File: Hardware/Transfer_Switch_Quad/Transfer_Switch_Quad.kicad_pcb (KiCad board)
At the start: 2 copper layers, 100 x 100 mm, 30 parts, among them J1 Relays, J10 RF1, J6 RF2, J7 RF3, J8 AMP, J9 RF4, K10 G2RL-1-E, K11 G2RL-1-E, K12 G2RL-1-E, K13 G2RL-1-E, K14 G2RL-1-E, K15 G2RL-1-E, K16 G2RL-1-E, K9 G2RL-1-E

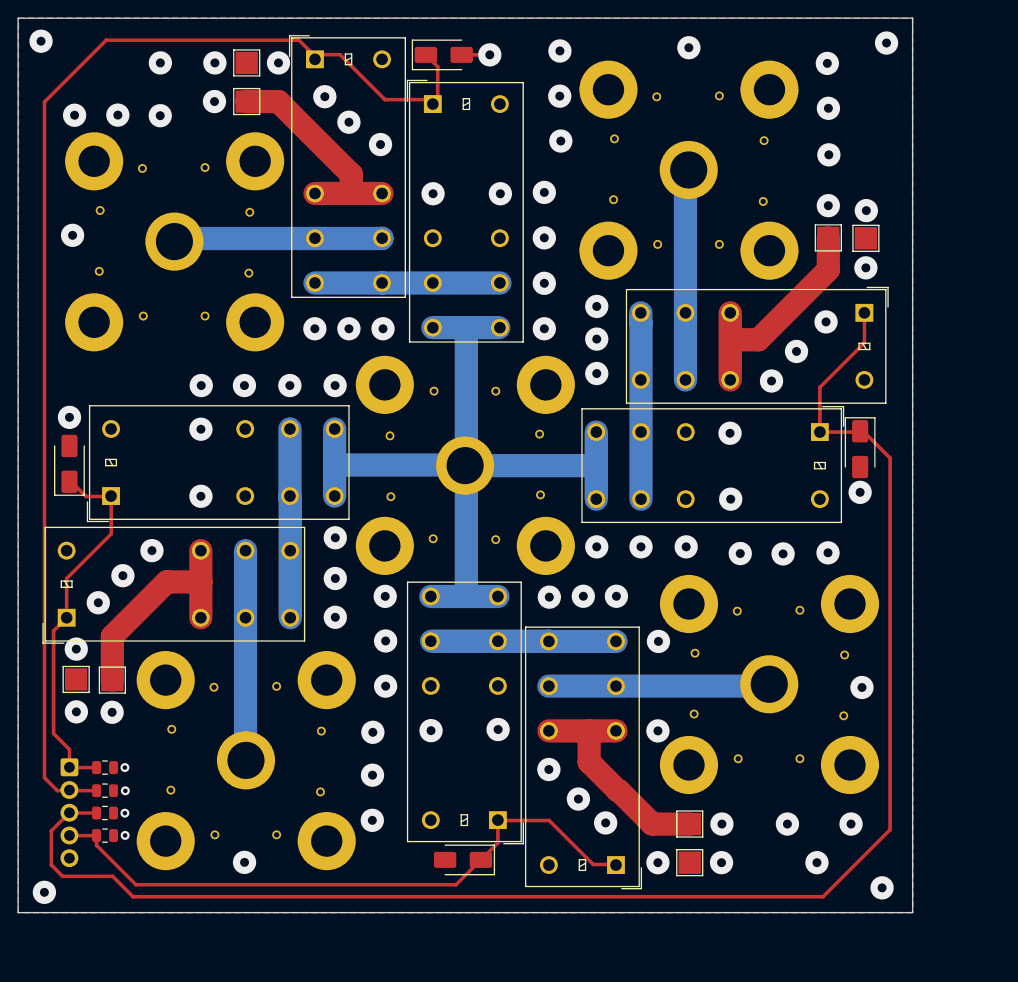
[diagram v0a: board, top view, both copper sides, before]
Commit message: SO-239 mount directly to the bottom of the pcb, so large hole and jumper to pad
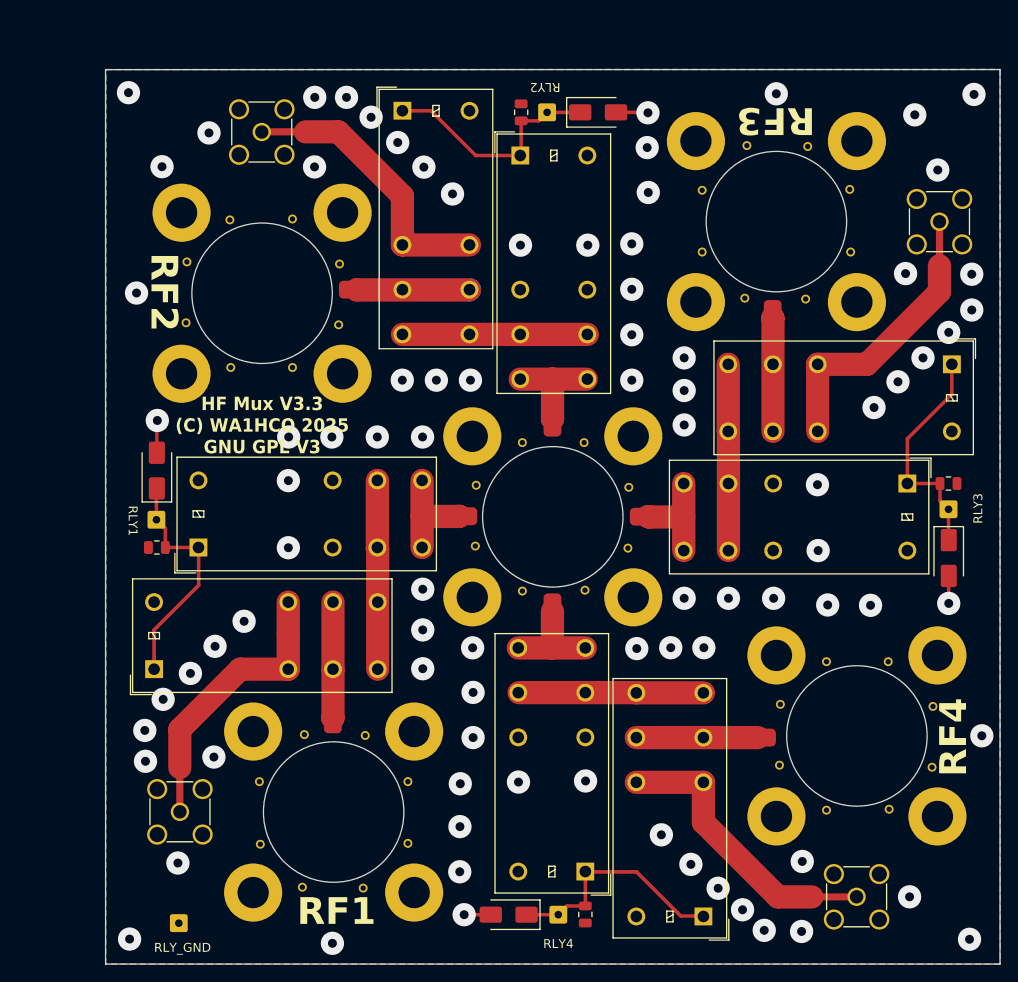
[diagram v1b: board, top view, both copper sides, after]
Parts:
- removed the J1 at (51.0, 128.0)
- removed TP16: Jump3, TestPoint:TestPoint_Pad_2.5x2.5mm
- removed TP17, TP25, TP6, TP7: GND, TestPoint:TestPoint_Pad_2.5x2.5mm
- removed TP20: Jump4, TestPoint:TestPoint_Pad_2.5x2.5mm
- removed TP24: Jump2, TestPoint:TestPoint_Pad_2.5x2.5mm
- removed TP5: Jump1, TestPoint:TestPoint_Pad_2.5x2.5mm
- added J10: Coax1, Connector_Coaxial:SMA_Amphenol_901-144_Vertical, F.Cu at (63.4, 133.0)
- added J7: Coax2, Connector_Coaxial:SMA_Amphenol_901-144_Vertical, F.Cu at (72.5, 57.0)
- added J8: Coax3, Connector_Coaxial:SMA_Amphenol_901-144_Vertical, F.Cu at (148.3, 67.0)
- added J9: Coax4, Connector_Coaxial:SMA_Amphenol_901-144_Vertical, F.Cu at (139.1, 142.5)
- added PAD1: PAD2X4, Connector_Wire:SolderWirePad_1x01_SMD_2x4mm, F.Cu at (80.5, 122.2)
- added PAD2: PAD2X4, Connector_Wire:SolderWirePad_1x01_SMD_2x4mm, F.Cu at (83.2, 74.6)
- added PAD3: PAD2X4, Connector_Wire:SolderWirePad_1x01_SMD_2x4mm, F.Cu at (129.7, 77.8)
- added PAD4: PAD2X4, Connector_Wire:SolderWirePad_1x01_SMD_2x4mm, F.Cu at (128.0, 124.7)
- added PAD5: PAD2X4, Connector_Wire:SolderWirePad_1x01_SMD_2x4mm, F.Cu at (94.7, 100.0)
- added PAD6: PAD2X4, Connector_Wire:SolderWirePad_1x01_SMD_2x4mm, F.Cu at (105.0, 89.0)
- added PAD7: PAD2X4, Connector_Wire:SolderWirePad_1x01_SMD_2x4mm, F.Cu at (115.7, 100.0)
- added PAD8: PAD2X4, Connector_Wire:SolderWirePad_1x01_SMD_2x4mm, F.Cu at (105.0, 110.6)
- added RLY1: ~, Connector_Wire:SolderWire-0.25sqmm_1x01_D0.65mm_OD2mm, F.Cu at (60.8, 100.3)
- added RLY2: ~, Connector_Wire:SolderWire-0.25sqmm_1x01_D0.65mm_OD2mm, F.Cu at (104.5, 54.8)
- added RLY3: ~, Connector_Wire:SolderWire-0.25sqmm_1x01_D0.65mm_OD2mm, F.Cu at (149.3, 99.2)
- added RLY4: ~, Connector_Wire:SolderWire-0.25sqmm_1x01_D0.65mm_OD2mm, F.Cu at (105.7, 144.5)
- added RLY5: ~, Connector_Wire:SolderWire-0.25sqmm_1x01_D0.65mm_OD2mm, F.Cu at (63.3, 145.4)
- J1: renamed from J7; footprint Relay_4to1:UHF_SO-239_Pin -> Relay_4to1:UHF_SO-239_hole
- J2: renamed from J6; footprint Relay_4to1:UHF_SO-239_Pin -> Relay_4to1:UHF_SO-239_hole
- J3: renamed from J8; footprint Relay_4to1:UHF_SO-239_Pin -> Relay_4to1:UHF_SO-239_hole; moved to B.Cu
- J4: renamed from J9; footprint Relay_4to1:UHF_SO-239_Pin -> Relay_4to1:UHF_SO-239_hole
- J5: renamed from J10; footprint Relay_4to1:UHF_SO-239_Pin -> Relay_4to1:UHF_SO-239_hole
- moved C3 101.2 mm to (149.3, 96.3)
- moved C2 89.0 mm to (101.5, 54.8), turned to 90 degrees
- moved C4 54.4 mm to (108.7, 144.5), turned to -90 degrees
- moved C1 25.3 mm to (60.8, 103.5), turned to 180 degrees
- moved D1 18.4 mm to (110.2, 54.8)
- moved D3 15.7 mm to (149.3, 104.6)
- moved J1 11.3 mm to (130.1, 67.0), turned to 0 degrees
- moved J2 11.3 mm to (72.6, 75.0)
- moved J3 11.3 mm to (105.1, 100.0)
- moved J4 11.3 mm to (139.1, 124.5), turned to -90 degrees
- moved K1 11.3 mm to (88.3, 54.6)
- moved K3 11.3 mm to (101.5, 59.6)
- moved K5 11.3 mm to (144.7, 96.3)
- moved J5 11.3 mm to (80.6, 133.0), turned to 180 degrees
- moved K7 11.3 mm to (60.5, 117.1)
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- renumbered C4 to C1, C3 to C2, C2 to C3, C1 to C4, D3 to D1, D4 to D2, D2 to D3, D1 to D4, K16 to K1, K14 to K2, K12 to K3, K9 to K4, K11 to K5, K10 to K6, K13 to K7, K15 to K8
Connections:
- K1 pad 11: Net-(J6-In) -> Net-(K1-Pad11)
- K2 pad 11: Net-(J7-In) (its old number) -> Net-(K2-Pad11)
- K3 pad 14: Net-(J8-In) (its old number) -> Net-(K3-Pad14)
- K4 pad 14: Net-(J8-In) (its old number) -> Net-(K4-Pad14)
- K5 pad 14: Net-(J8-In) (its old number) -> Net-(K5-Pad14)
- K6 pad 14: Net-(J8-In) (its old number) -> Net-(K6-Pad14)
- K7 pad 11: Net-(J10-In) (its old number) -> Net-(K7-Pad11)
- K8 pad 11: Net-(J9-In) (its old number) -> Net-(K8-Pad11)
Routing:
- net /RLY3: track 174.0 -> 25.8 mm
- net /RLY2: track 137.3 -> 26.2 mm
- net Net-(J8-In) (its old number): track 89.2 -> 0.00 mm
- net /RLY4: track 70.5 -> 26.1 mm
- net Net-(J9-In) (its old number): track 24.8 -> 0.00 mm
- net Net-(J10-In) (its old number): track 23.5 -> 0.00 mm
- net Net-(J7-In) (its old number): track 23.4 -> 0.00 mm
- net Net-(J6-In): track 23.0 -> 0.00 mm
- net /RLY1: track 42.4 -> 26.4 mm
- net Net-(K8-Pad11): track 0.00 -> 13.6 mm
- net Net-(K7-Pad11): track 0.00 -> 12.7 mm
- net Net-(K2-Pad11): track 0.00 -> 12.7 mm
- net Net-(K1-Pad11): track 0.00 -> 12.6 mm
- net Net-(K3-Pad14): track 0.00 -> 11.8 mm
- net Net-(K4-Pad14): track 0.00 -> 11.7 mm
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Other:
- board text added: "April 17, 2026"
- board text added: "HF Mux"
- board text added: "HF Mux V3.3 (C) WA1HCO 2025 GNU GPL V3"
- board text added: "HF multiplexer with bypass for ports not selected. Two boards make a 4:1 multiplexer with high isolation. Enable 4 radios to use 4 antennas witht the amplifier connected inline with the active transmitter."
- board text added: "RF2"
- board text added: "RLY1"
- board text added: "RLY2"
- board text added: "RLY3"
- board text added: "RLY4"
- board text added: "RLY_GND"
- board text added: "V3.2"
- board text removed: "(C) WA1HCO 2025"
- board text removed: "AMP"
- board text removed: "GNU GPLv3"
